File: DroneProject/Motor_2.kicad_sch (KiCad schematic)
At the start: 0 parts

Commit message: Finished motor and C1 designs, still need to rename components on MTR2, 3, and 4 pages
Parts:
- added C1, C4: 1uF, Capacitor_SMD:C_0402_1005Metric, symbol Device:C
- added C10, C11, C12, C14, C15, C9: 1uF, Capacitor_SMD:C_0603_1608Metric, symbol Device:C
- added C13, C16, C3: 0.1uF, Capacitor_SMD:C_0402_1005Metric, symbol Device:C
- added C2: 10uF, Capacitor_SMD:C_1206_3216Metric, symbol Device:C
- added C6: 47nF, Capacitor_SMD:C_0402_1005Metric, symbol Device:C
- added C7, C8: 270uF, Capacitor_SMD:CP_Elec_10x10.5, symbol Device:C_Polarized
- added NT1, NT2, NT3, NT4: NetTie_2, NetTie:NetTie-2_SMD_Pad0.5mm, symbol Device:NetTie_2
- added Q1, Q2, Q3, Q4, Q5, Q6: CSD17577Q5A, Package_TO_SOT_SMD:TDSON-8-1, symbol Transistor_FET:CSD17577Q5A
- added R1, R2, R3: 10K, Resistor_SMD:R_0402_1005Metric, symbol Device:R_US
- added R4: 33, Resistor_SMD:R_0402_1005Metric, symbol Device:R_US
- added R5, R6: CSS2H-2512K-2L00J, Resistor_SMD:R_2512_6332Metric, symbol Device:R
- added U1: DRV8320SRTVR, Library:DRV8320SRTVR, symbol Global:DRV8320SRTVR
- added U2, U3: INA180A2, Package_TO_SOT_SMD:SOT-23-5, symbol Amplifier_Current:INA180A2
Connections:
- new net: NT1.2, U2.3 (+)
- new net: NT2.2, U2.4 (-)
- new net: NT1.1, Q2.1 (S), Q2.2 (S), Q2.3 (S), R5.1, U1.8 (SLA)
- new net: NT3.1, Q4.1 (S), Q4.2 (S), Q4.3 (S), R6.1, U1.9 (SLB)
- new net: Q4.4 (G), U1.10 (GLB)
- new net: Q2.4 (G), U1.7 (GLA)
- new net: C4.2, U1.2 (VCP)
- new net: R4.2, U1.18 (SDO)
- new net: C6.2, U1.1 (CPH)
- new net: Q3.4 (G), U1.12 (GHB)
- new net: Q5.4 (G), U1.13 (GHC)
- new net: Q6.4 (G), U1.15 (GLC)
- new net: C6.1, U1.32 (CPL)
- new net: Q1.4 (G), U1.5 (GHA)
- new net: NT3.2, U3.3 (+)
- new net: NT4.2, U3.4 (-)
- new net +3.3V: C13.1, C16.1, R1.2, R2.2, R3.2, U2.5 (V+), U3.5 (V+)
- new net C1_SPI2_MISO: R4.1
- new net C1_SPI2_MOSI: U1.19 (SDI)
- new net C1_SPI2_SCK: U1.20 (SCK)
- new net GND: C1.2, C13.2, C16.2, U1.23 (AGND), U1.33 (PAD), U2.2 (GND), U3.2 (GND)
- new net GNDPWR: C10.2, C11.2, C12.2, C14.2, C15.2, C2.2, C3.2, C7.2, C8.2, C9.2, NT2.1, NT4.1, Q6.1 (S), Q6.2 (S), Q6.3 (S), R5.2, R6.2, U1.16 (SLC), U1.31 (PGND)
- new net MTR1_DVDD: C1.1, U1.24 (DVDD)
- new net MTR2_A: Q1.1 (S), Q1.2 (S), Q1.3 (S), Q2.5 (D), U1.6 (SHA)
- new net MTR2_A_PWM: U1.25 (INHA)
- new net MTR2_B: Q3.1 (S), Q3.2 (S), Q3.3 (S), Q4.5 (D), U1.11 (SHB)
- new net MTR2_B_PWM: U1.27 (INHB)
- new net MTR2_C: Q5.1 (S), Q5.2 (S), Q5.3 (S), Q6.5 (D), U1.14 (SHC)
- new net MTR2_CSN: R3.1, U1.21 (nSCS)
- new net MTR2_CURR_A: U2.1
- new net MTR2_CURR_B: U3.1
- new net MTR2_C_PWM: U1.29 (INHC)
- new net MTR2_EN: R2.1, U1.22 (ENABLE)
- new net MTR2_FAULT_N: R1.1, U1.17 (FAULT_N)
- new net VDD: C10.1, C11.1, C12.1, C14.1, C15.1, C2.1, C3.1, C4.1, C7.1, C8.1, C9.1, Q1.5 (D), Q3.5 (D), Q5.5 (D), U1.3 (VM), U1.4 (VDRAIN)

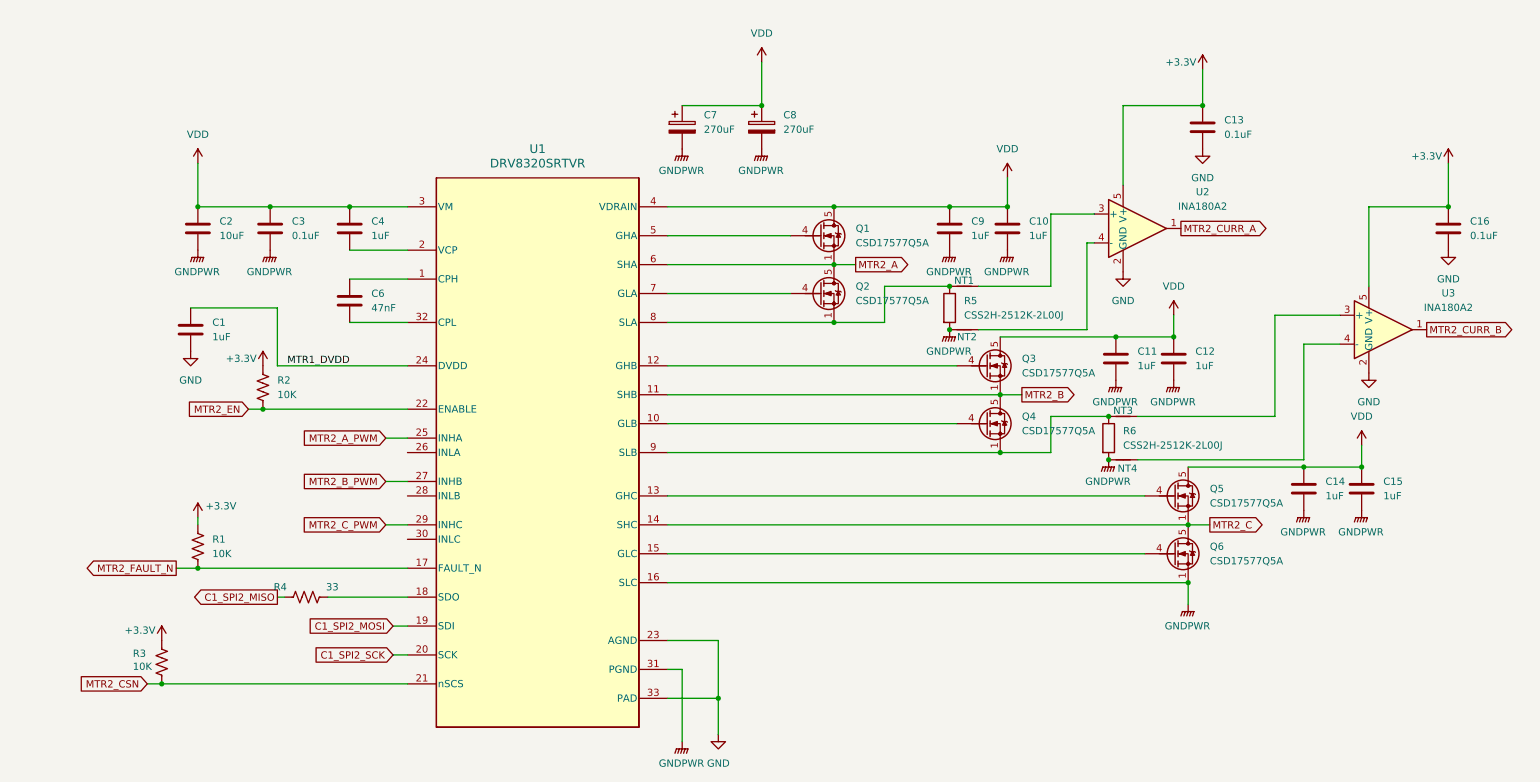
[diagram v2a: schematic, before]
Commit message: Finished most of routing for motor controls, however likely going to revert back and make separate ESC boards for motor control as I think that would honestly be more efficient from both a cost and debug complexity standpoint.
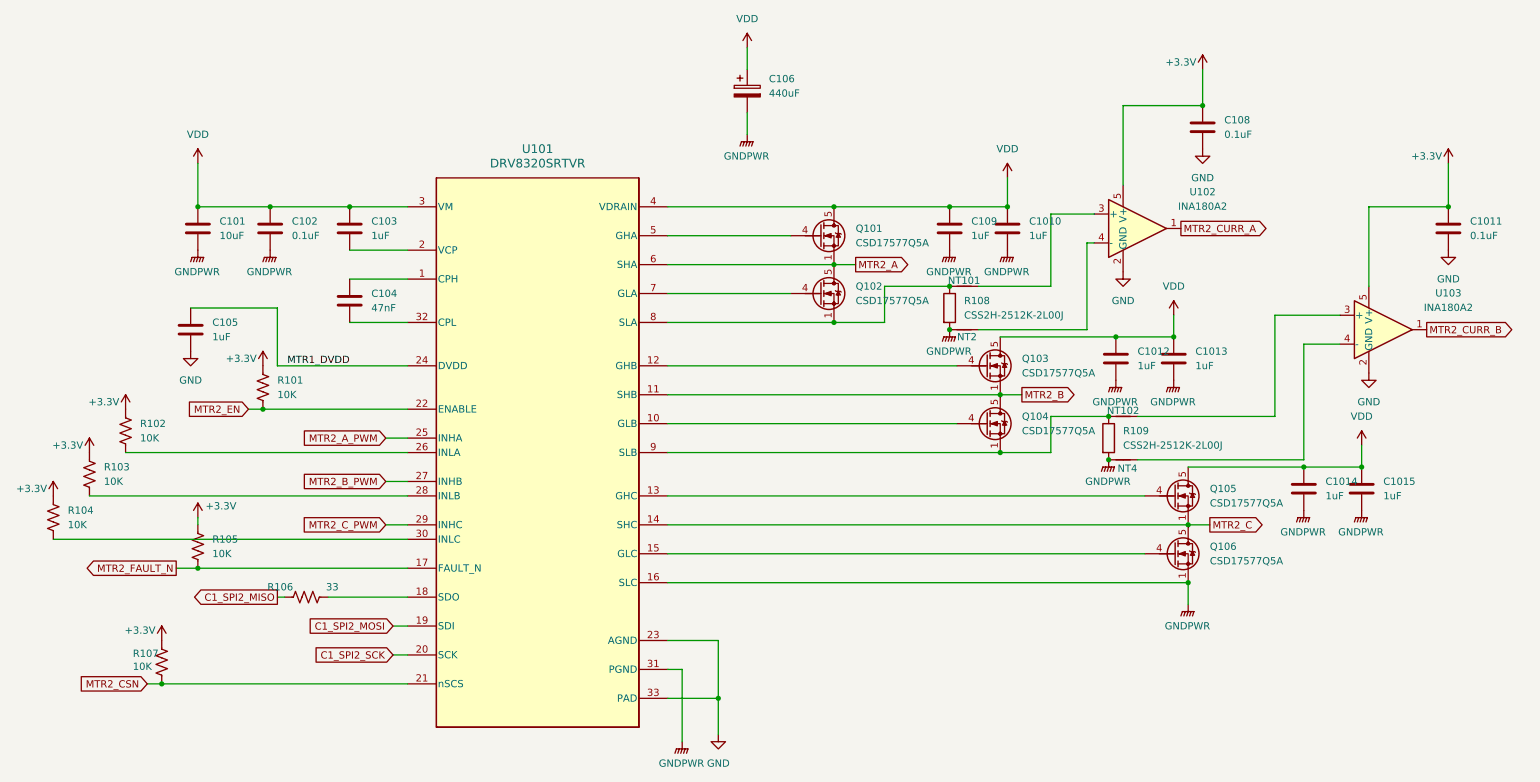
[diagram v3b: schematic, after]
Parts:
- removed C7, C8: 270uF, Capacitor_SMD:CP_Elec_10x10.5, symbol Device:C_Polarized
- added C106: 440uF, Capacitor_THT:CP_Radial_D10.0mm_P5.00mm, symbol Device:C_Polarized
- added R102, R103, R104: 10K, Resistor_SMD:R_0402_1005Metric, symbol Device:R_US
- renumbered C2 to C101, C10 to C1010, C16 to C1011, C11 to C1012, C12 to C1013, C14 to C1014, C15 to C1015, C3 to C102, C4 to C103, C6 to C104, C1 to C105, C13 to C108, C9 to C109, NT1 to NT101, NT3 to NT102, Q1 to Q101, Q2 to Q102, Q3 to Q103, Q4 to Q104, Q5 to Q105, Q6 to Q106, R2 to R101, R1 to R105, R4 to R106, R3 to R107, R5 to R108, R6 to R109, U1 to U101, U2 to U102, U3 to U103
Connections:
- net +3.3V: now also R102.2, R103.2, R104.2
- net GNDPWR: now also C106.2
- net VDD: now also C106.1
- net at U101.26 (INLA): now also R102.1
- net at U101.28 (INLB): now also R103.1
- net at U101.30 (INLC): now also R104.1
